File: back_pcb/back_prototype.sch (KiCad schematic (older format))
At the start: 79 parts, among them P1 EXPANSION_LEFT, P10 CONN_01X08, P2 EXPANSION_BOTTOM, P3 EXPANSION_TOP, P4 USB_A, P5 AUDIO_CONN, P6 ATMEGA_HEADER, P7 EXPANSION_BOTTOM2, P8 JST, P9 USB_A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

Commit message: Resolved the sch symbol replacement dialog
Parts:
- P4, P9: symbol USB_A -> USB_A-RESCUE-back_prototype
- U3: symbol MCP23017 -> MCP23017-RESCUE-back_prototype
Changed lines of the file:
@@
 EESchema Schematic File Version 2
+LIBS:back_prototype-rescue
 LIBS:power
 LIBS:device
@@
 SIM800_DTR
 $Comp
-L MCP23017 U3
+L MCP23017-RESCUE-back_prototype U3
 U 1 1 5888D7F8
 P 5750 1850
@@
 SDA
 $Comp
-L USB_A P4
+L USB_A-RESCUE-back_prototype P4
 U 1 1 588A9EDA
 P 10750 3850
@@
 $EndComp
 $Comp
-L USB_A P9
+L USB_A-RESCUE-back_prototype P9
 U 1 1 58C9652A
 P 10750 4600

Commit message: Re-thought and re-traced 13-pin header pinout
I2S part will likely get changed later, too
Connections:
- net +3V3: now also P1.9 (P9); no longer P1.13 (P13)
- net CS: now also P1.10 (P10); no longer P1.8 (P8)
- net GND: now also P1.8 (P8); no longer P1.12 (P12)
- net MISO: now also P1.12 (P12); no longer P1.10 (P10)
- net MOSI: now also P1.13 (P13); no longer P1.11 (P11)
- net SCK: now also P1.11 (P11); no longer P1.9 (P9)
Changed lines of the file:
@@
 Text GLabel 2450 4900 2    60   Input ~ 0
 CS
+Text GLabel 4700 6450 0    60   Input ~ 0
+MOSI
+Text GLabel 4700 6350 0    60   Input ~ 0
+MISO
 Text GLabel 4700 6250 0    60   Input ~ 0
-MOSI
+SCK
 Text GLabel 4700 6150 0    60   Input ~ 0
-MISO
-Text GLabel 4700 6050 0    60   Input ~ 0
-SCK
-Text GLabel 4700 5950 0    60   Input ~ 0
 CS
 NoConn ~ 2450 4800
@@
 L +3.3V #PWR028
 U 1 1 58896BBB
-P 4700 6450
-F 0 "#PWR028" H 4700 6300 50  0001 C CNN
-F 1 "+3.3V" V 4700 6750 50  0000 C CNN
-F 2 "" H 4700 6450 50  0000 C CNN
-F 3 "" H 4700 6450 50  0000 C CNN
-	1    4700 6450
+P 4700 6050
+F 0 "#PWR028" H 4700 5900 50  0001 C CNN
+F 1 "+3.3V" V 4700 6350 50  0000 C CNN
+F 2 "" H 4700 6050 50  0000 C CNN
+F 3 "" H 4700 6050 50  0000 C CNN
+	1    4700 6050
 	0    -1   -1   0
 $EndComp
@@
 L GND #PWR029
 U 1 1 58896C98
-P 4700 6350
-F 0 "#PWR029" H 4700 6100 50  0001 C CNN
-F 1 "GND" V 4700 6100 50  0000 C CNN
-F 2 "" H 4700 6350 50  0000 C CNN
-F 3 "" H 4700 6350 50  0000 C CNN
-	1    4700 6350
+P 4700 5950
+F 0 "#PWR029" H 4700 5700 50  0001 C CNN
+F 1 "GND" V 4700 5700 50  0000 C CNN
+F 2 "" H 4700 5950 50  0000 C CNN
+F 3 "" H 4700 5950 50  0000 C CNN
+	1    4700 5950
 	0    1    1    0
 $EndComp

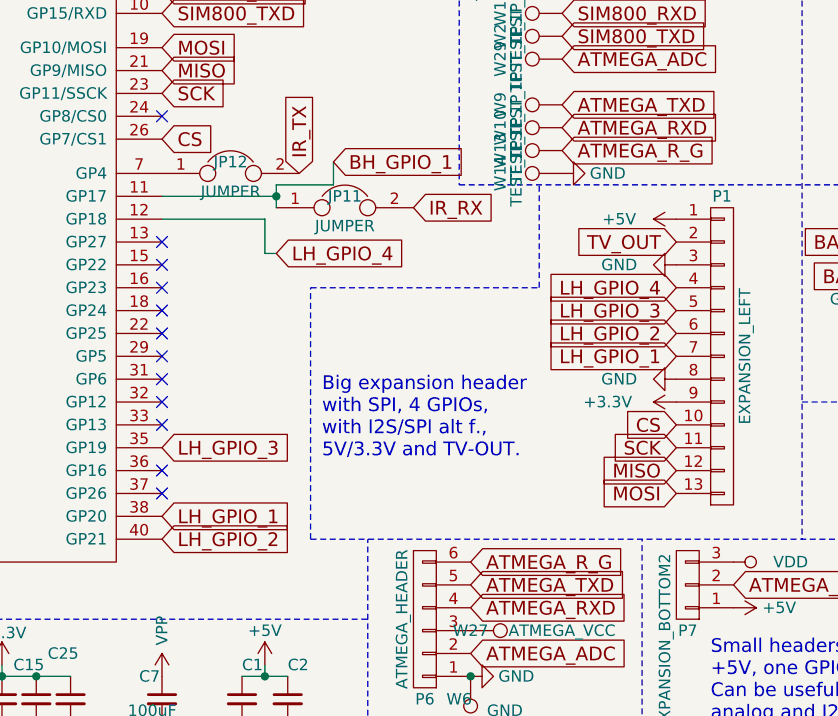
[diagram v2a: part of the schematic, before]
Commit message: Side header labels renamed to I2S pin names
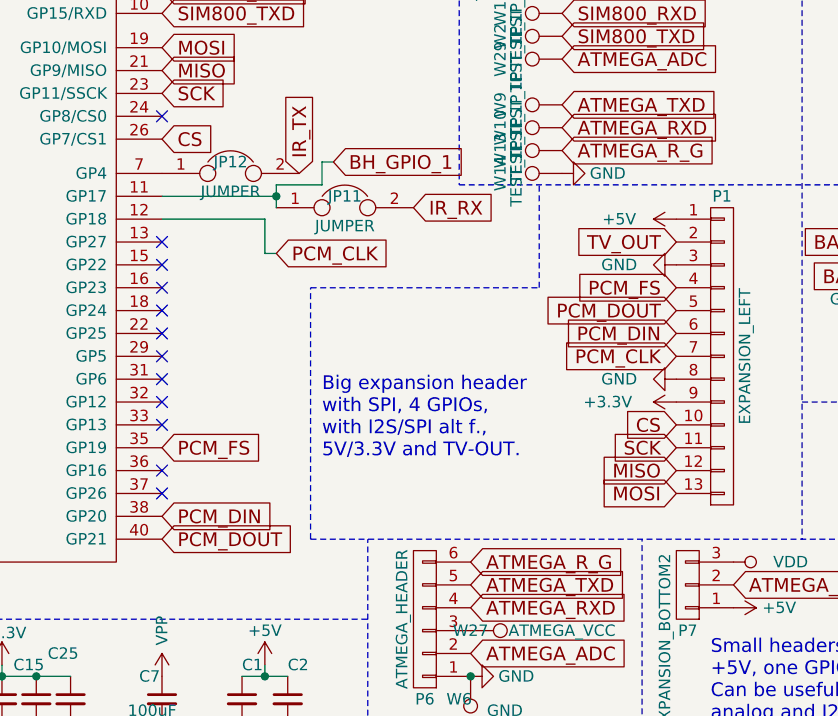
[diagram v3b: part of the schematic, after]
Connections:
- net LH_GPIO_1 renamed PCM_CLK
- net PCM_CLK: now also U1.12 (GP18); no longer U1.38 (GP20)
- net LH_GPIO_2 renamed PCM_DIN
- net PCM_DIN: now also U1.38 (GP20); no longer U1.40 (GP21)
- net LH_GPIO_3 renamed PCM_DOUT
- net PCM_DOUT: now also U1.40 (GP21); no longer U1.35 (GP19)
- net LH_GPIO_4 renamed PCM_FS
- net PCM_FS: now also U1.35 (GP19); no longer U1.12 (GP18)
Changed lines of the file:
@@
 $EndComp
 Text GLabel 2450 6650 2    60   Input ~ 0
-LH_GPIO_2
-Text GLabel 4700 5850 0    60   Input ~ 0
-LH_GPIO_1
+PCM_DOUT
 Text GLabel 4700 5750 0    60   Input ~ 0
-LH_GPIO_2
+PCM_DIN
+Text GLabel 4700 5650 0    60   Input ~ 0
+PCM_DOUT
 Text Notes 3150 6300 0    60   ~ 0
 Big expansion header \nwith SPI, 4 GPIOs, \nwith I2S/SPI alt f.,\n5V/3.3V and TV-OUT.
@@
 NoConn ~ 2450 6050
 Text GLabel 2450 6550 2    60   Input ~ 0
-LH_GPIO_1
+PCM_DIN
 Text GLabel 2450 6250 2    60   Input ~ 0
-LH_GPIO_3
-Text GLabel 4700 5650 0    60   Input ~ 0
-LH_GPIO_3
+PCM_FS
+Text GLabel 4700 5550 0    60   Input ~ 0
+PCM_FS
 $Comp
 L CONN_01X03 P7
@@
 BH_GPIO_1
 Text GLabel 2950 5400 2    60   Input ~ 0
-LH_GPIO_4
+PCM_CLK
 Connection ~ 2950 5150
 NoConn ~ 2450 6350
@@
 Wire Wire Line
 	2050 7450 1600 7450
-Text GLabel 4700 5550 0    60   Input ~ 0
-LH_GPIO_4
+Text GLabel 4700 5850 0    60   Input ~ 0
+PCM_CLK
 NoConn ~ 5150 1750
 NoConn ~ 5150 1650
@@
 Wire Wire Line
 	2900 5400 2900 5250
-Wire Wire Line
-	2950 5100 3200 5100
-Wire Wire Line
-	3200 5100 3200 5000
 $Comp
 L JUMPER3 JP8
@@
 $EndComp
 Connection ~ 10450 2500
+Wire Wire Line
+	3200 5000 3150 5000
+Wire Wire Line
+	3150 5000 3150 5100
+Wire Wire Line
+	3150 5100 2950 5100
 $EndSCHEMATC

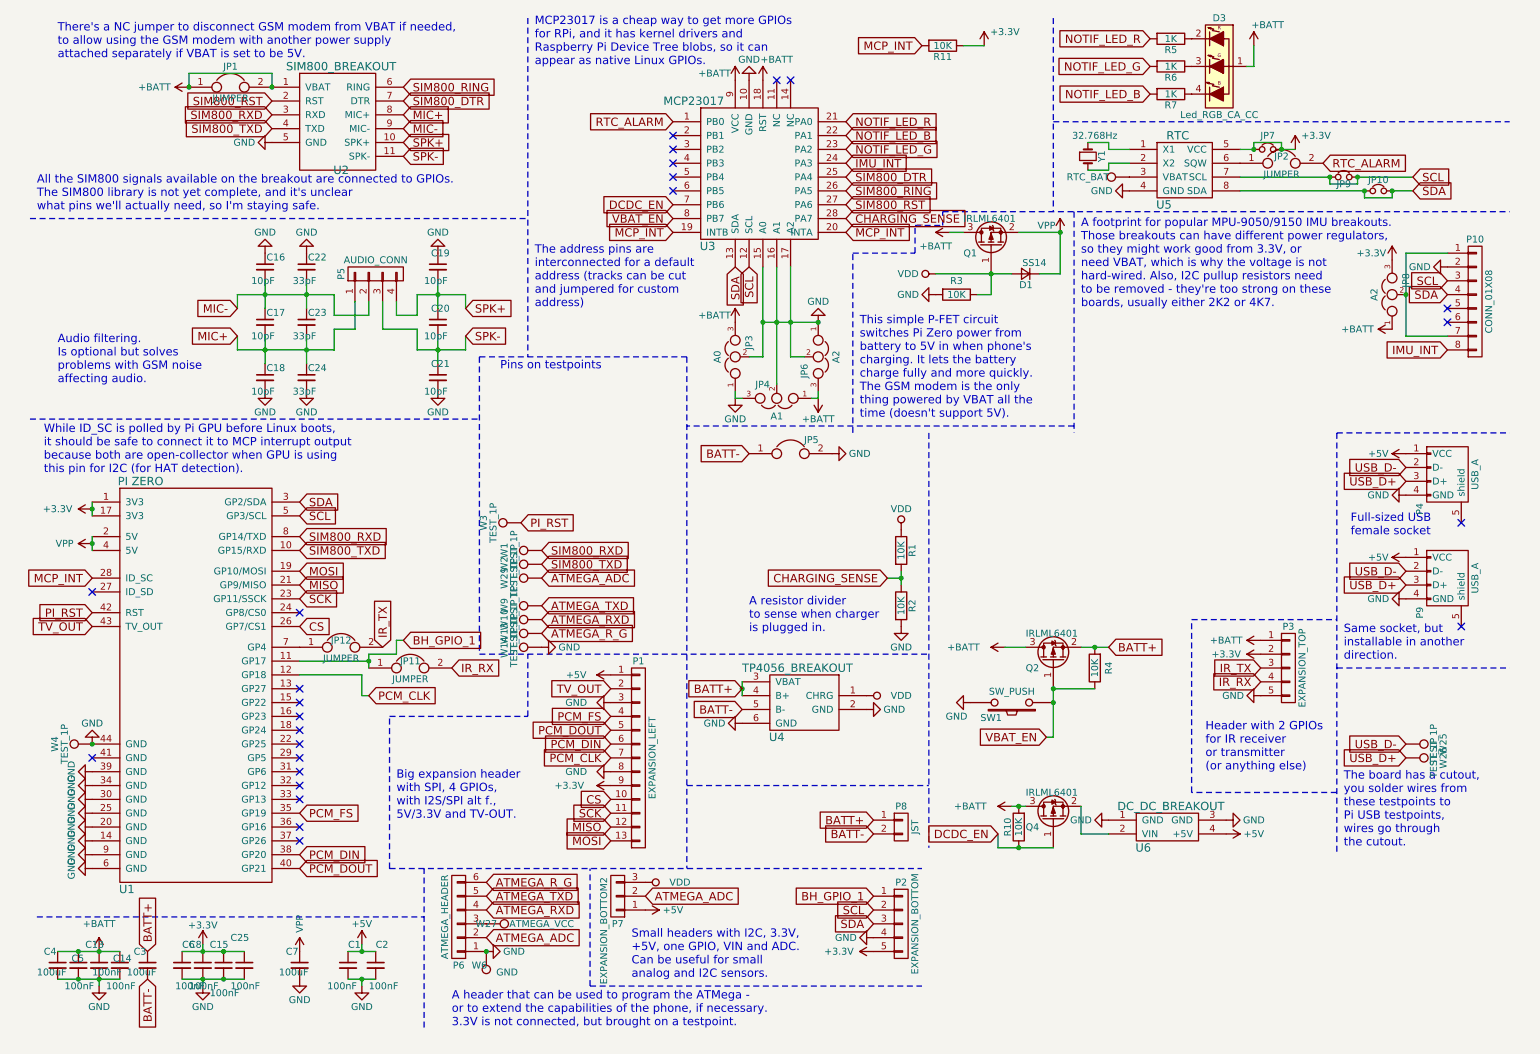
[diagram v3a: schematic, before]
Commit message: GSM modem and removing features
-Flipped the GSM modem, improving the board dramatically
-Removed MPU-9150 header
-Removed RTC footprint
-Removed board center-facing USB port
-Added inductors in series with microphone (not yet added to the PCB)
-Swapped pins of the IR header so that plugging an IR expansion board in
reverse wouldn't kill it
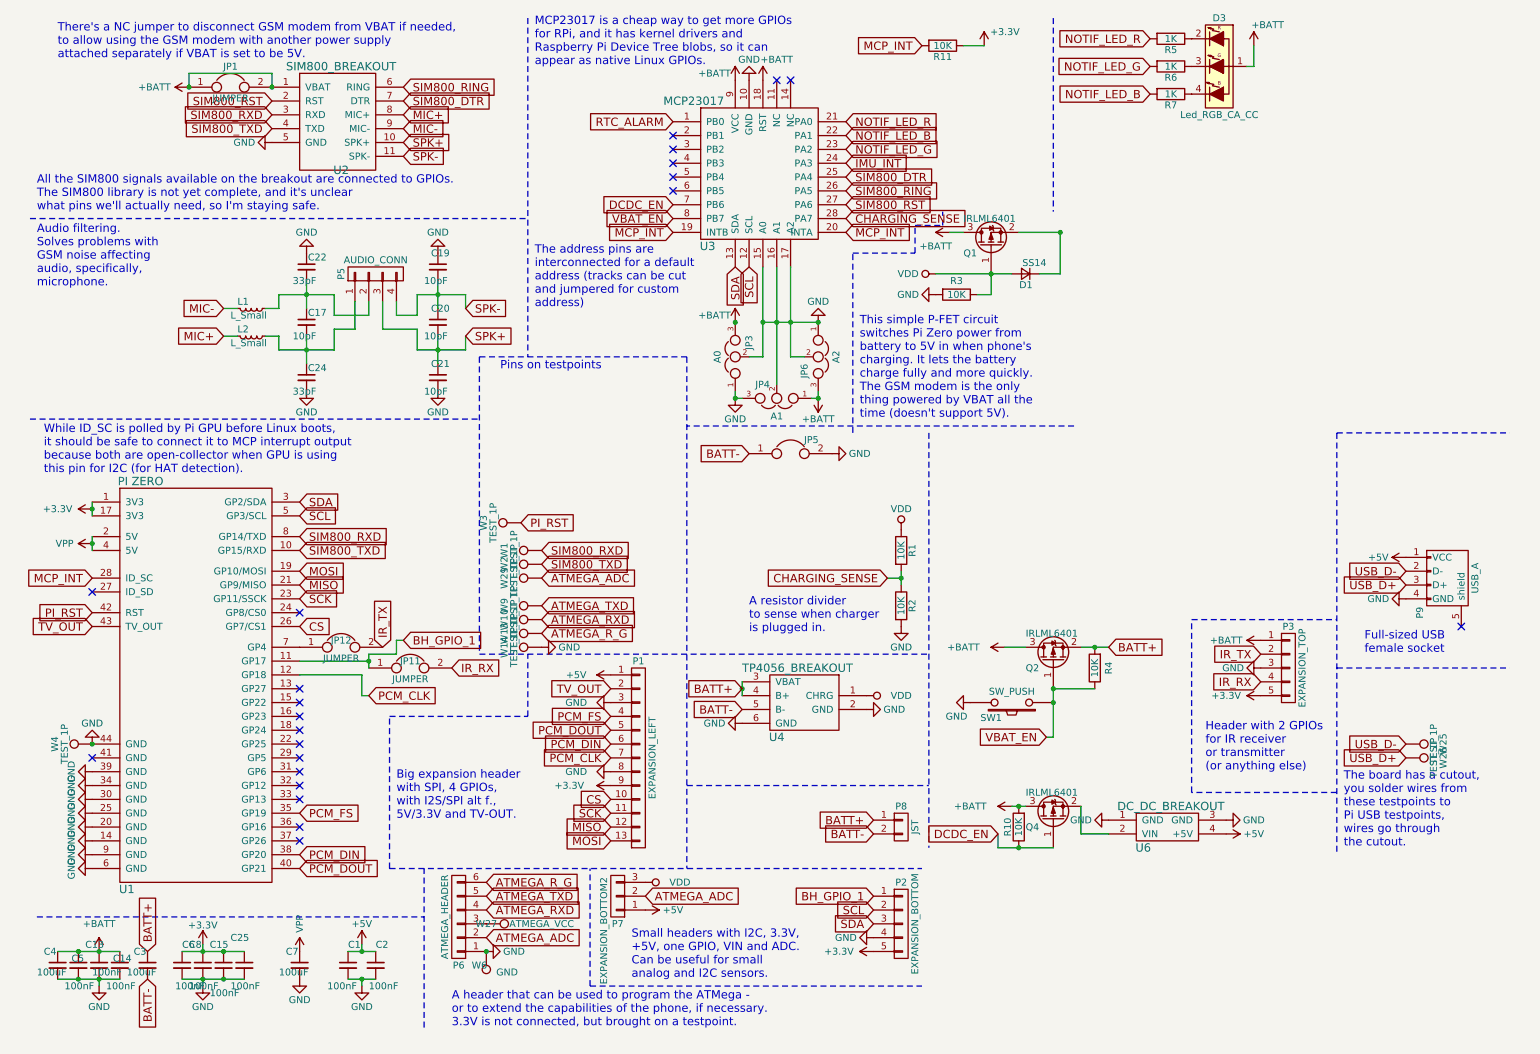
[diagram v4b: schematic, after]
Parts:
- removed C16, C18: 10pF, Capacitors_SMD:C_0603_HandSoldering, symbol C_Small
- removed C23: 33pF, Capacitors_SMD:C_0603_HandSoldering, symbol C_Small
- removed JP10, JP7, JP9: Jumper_NC_Small, common-footprints:GS2_SMALL, symbol Jumper_NC_Small
- removed JP2: JUMPER, common-footprints:GS2_SMALL, symbol JUMPER
- removed JP8: A2, common-footprints:GS3_SMALL, symbol JUMPER3
- removed P10: CONN_01X08, Pin_Headers:Pin_Header_Straight_1x08_Pitch2.54mm, symbol CONN_01X08
- removed P4: USB_A, footprints:USB_A, symbol USB_A-RESCUE-back_prototype
- removed U5: RTC, Housings_SOIC:SOIC-8_3.9x4.9mm_Pitch1.27mm, symbol RTC
- removed W15: RTC_BAT, Measurement_Points:Measurement_Point_Square-SMD-Pad_Small, symbol TEST_1P
- removed Y1: 32.768Hz, Crystals:Crystal_SMD_G8-2pin_3.2x1.5mm_HandSoldering, symbol Crystal_Small
- added L1, L2: L_Small, Resistors_SMD:R_0603_HandSoldering, symbol L_Small
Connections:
- net +3V3: now also P3.5 (P5); no longer P3.2 (P2)
- net GND: now also P3.3 (P3); no longer P3.5 (P5)
- net IR_TX: now also P3.2 (P2); no longer P3.3 (P3)
- net MIC+: now also L2.2; no longer C17.2, C24.1, P5.1 (P1)
- net MIC-: now also L1.2; no longer C17.1, C22.2, P5.2 (P2)
- net SPK+: now also C20.2, C21.1, P5.3 (P3); no longer C19.2, C20.1, P5.4 (P4)
- net SPK-: now also C19.2, C20.1, P5.4 (P4); no longer C20.2, C21.1, P5.3 (P3)
- net VPP: no longer D1.1 (K), Q1.2 (S)
- new net: C17.1, C22.2, L1.1, P5.2 (P2)
- new net: C17.2, C24.1, L2.1, P5.1 (P1)
- new net: D1.1 (K), Q1.2 (S)
- no-connect marks 25 -> 22
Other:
- note added: "Audio filtering.\nSolves problems with \nGSM noise affecting \naudio, specifically,\nmicrophone."
- note removed: "A footprint for popular MPU-9050/9150 IMU breakouts.\nThose breakouts can have different power regulators,\nso they might work good from 3.3V, or \nneed VBAT, which is why the voltage is not \nhard-wired. Also, I2C pullup resistors need \nto be removed - they're too strong on these \nboards, usually either 2K2 or 4K7."
- note removed: "Audio filtering.\nIs optional but solves \nproblems with GSM noise\naffecting audio."
- note removed: "Same socket, but\ninstallable in another\ndirection."
- moved on the sheet: C17
